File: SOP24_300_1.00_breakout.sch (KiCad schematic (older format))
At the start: 9 parts, among them P1 SOP24-300-1.00, P2 CONN_12, P3 CONN_12, P4 CONN_1, P5 CONN_1, P6 CONN_1, P7 CONN_1

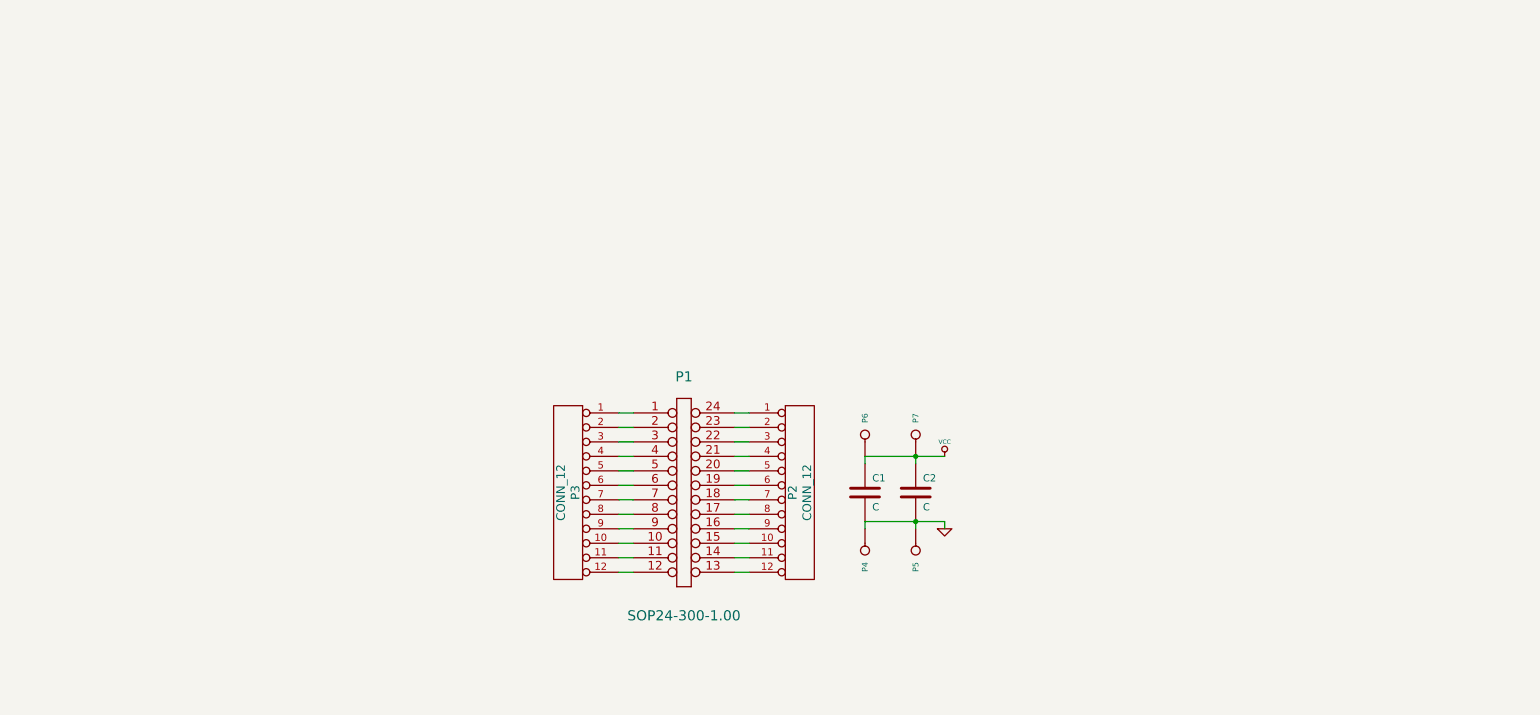
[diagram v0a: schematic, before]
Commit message: One step before adding the bridge-wires (DRC off).
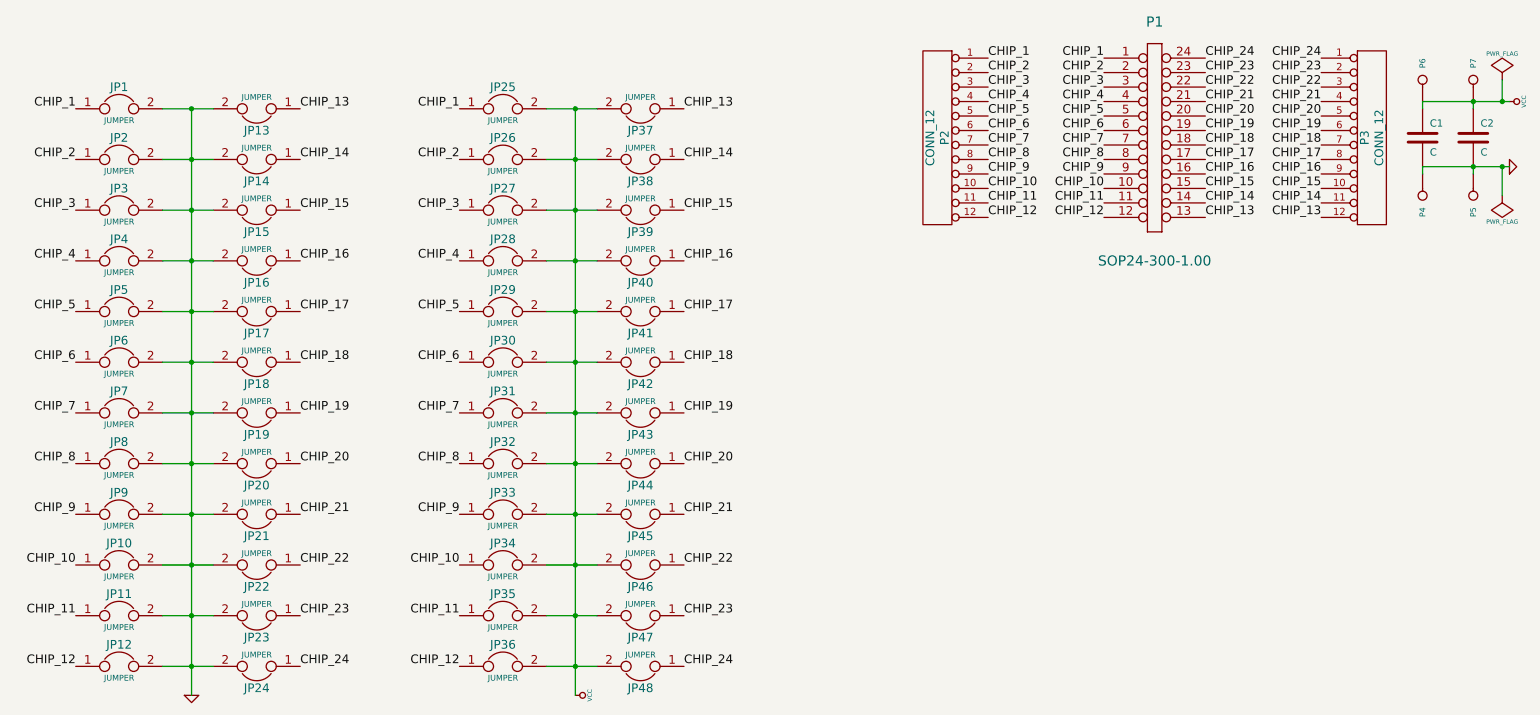
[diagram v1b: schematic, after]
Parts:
- added JP1, JP10, JP11, JP12, JP13, JP14, JP15, JP16, JP17, JP18, JP19, JP2, JP20, JP21, JP22, JP23, JP24, JP25, JP26, JP27, JP28, JP29, JP3, JP30, JP31, JP32, JP33, JP34, JP35, JP36, JP37, JP38, JP39, JP4, JP40, JP41, JP42, JP43, JP44, JP45, JP46, JP47, JP48, JP5, JP6, JP7, JP8, JP9: JUMPER, symbol JUMPER
- renumbered P3 to P2, P2 to P3
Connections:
- net GND: now also JP1.2, JP10.2, JP11.2, JP12.2, JP13.2, JP14.2, JP15.2, JP16.2, JP17.2, JP18.2, JP19.2, JP2.2, JP20.2, JP21.2, JP22.2, JP23.2, JP24.2, JP3.2, JP4.2, JP5.2, JP6.2, JP7.2, JP8.2, JP9.2
- net VCC: now also JP25.2, JP26.2, JP27.2, JP28.2, JP29.2, JP30.2, JP31.2, JP32.2, JP33.2, JP34.2, JP35.2, JP36.2, JP37.2, JP38.2, JP39.2, JP40.2, JP41.2, JP42.2, JP43.2, JP44.2, JP45.2, JP46.2, JP47.2, JP48.2
- net CHIP_24: now reaches P1.24 (P24), P3.1 (P1)
- net CHIP_24: now also JP24.1, JP48.1
- net CHIP_15: now reaches P1.15 (P15), P3.10 (P10)
- net CHIP_15: now also JP15.1, JP39.1
- net CHIP_14: now reaches P1.14 (P14), P3.11 (P11)
- net CHIP_14: now also JP14.1, JP38.1
- net CHIP_13: now reaches P1.13 (P13), P3.12 (P12)
- net CHIP_13: now also JP13.1, JP37.1
- net CHIP_23: now reaches P1.23 (P23), P3.2 (P2)
- net CHIP_23: now also JP23.1, JP47.1
- net CHIP_22: now reaches P1.22 (P22), P3.3 (P3)
- net CHIP_22: now also JP22.1, JP46.1
- net CHIP_21: now reaches P1.21 (P21), P3.4 (P4)
- net CHIP_21: now also JP21.1, JP45.1
- net CHIP_20: now reaches P1.20 (P20), P3.5 (P5)
- net CHIP_20: now also JP20.1, JP44.1
- net CHIP_19: now reaches P1.19 (P19), P3.6 (P6)
- net CHIP_19: now also JP19.1, JP43.1
- net CHIP_18: now reaches P1.18 (P18), P3.7 (P7)
- net CHIP_18: now also JP18.1, JP42.1
- net CHIP_17: now reaches P1.17 (P17), P3.8 (P8)
- net CHIP_17: now also JP17.1, JP41.1
- net CHIP_16: now reaches P1.16 (P16), P3.9 (P9)
- net CHIP_16: now also JP16.1, JP40.1
- net CHIP_1: now reaches P1.1 (P1), P2.1 (P1)
- net CHIP_1: now also JP1.1, JP25.1
- net CHIP_10: now reaches P1.10 (P10), P2.10 (P10)
- net CHIP_10: now also JP10.1, JP34.1
- net CHIP_11: now reaches P1.11 (P11), P2.11 (P11)
- net CHIP_11: now also JP11.1, JP35.1
- net CHIP_12: now reaches P1.12 (P12), P2.12 (P12)
- net CHIP_12: now also JP12.1, JP36.1
- net CHIP_2: now reaches P1.2 (P2), P2.2 (P2)
- net CHIP_2: now also JP2.1, JP26.1
- net CHIP_3: now reaches P1.3 (P3), P2.3 (P3)
- net CHIP_3: now also JP27.1, JP3.1
- net CHIP_4: now reaches P1.4 (P4), P2.4 (P4)
- net CHIP_4: now also JP28.1, JP4.1
- net CHIP_5: now reaches P1.5 (P5), P2.5 (P5)
- net CHIP_5: now also JP29.1, JP5.1
- net CHIP_6: now reaches P1.6 (P6), P2.6 (P6)
- net CHIP_6: now also JP30.1, JP6.1
- net CHIP_7: now reaches P1.7 (P7), P2.7 (P7)
- net CHIP_7: now also JP31.1, JP7.1
- net CHIP_8: now reaches P1.8 (P8), P2.8 (P8)
- net CHIP_8: now also JP32.1, JP8.1
- net CHIP_9: now reaches P1.9 (P9), P2.9 (P9)
- net CHIP_9: now also JP33.1, JP9.1
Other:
- moved on the sheet: C1, C2, P1, P2, P3, P4, P5, P6, P7
